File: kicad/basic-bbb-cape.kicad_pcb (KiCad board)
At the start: 2 copper layers, 54.6 x 86.4 mm, 2 parts, among them P8 BeagleBone_Black_Header, P9 BeagleBone_Black_Header

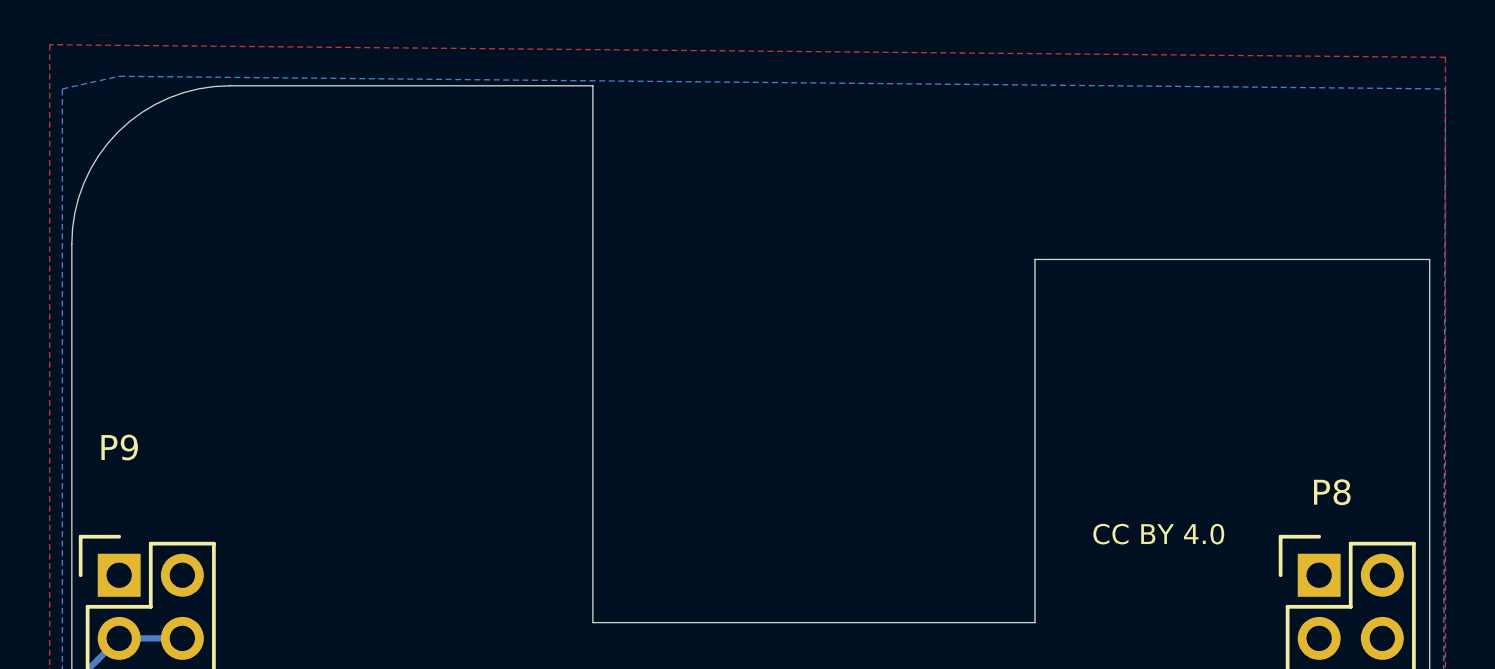
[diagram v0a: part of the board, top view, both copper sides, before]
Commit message: kicad: Multiple changes including adding
sym-lib-table,
Beaglebone_black_p8.kicad_sym, and
Beaglebone_black_p9.kicad_sym.
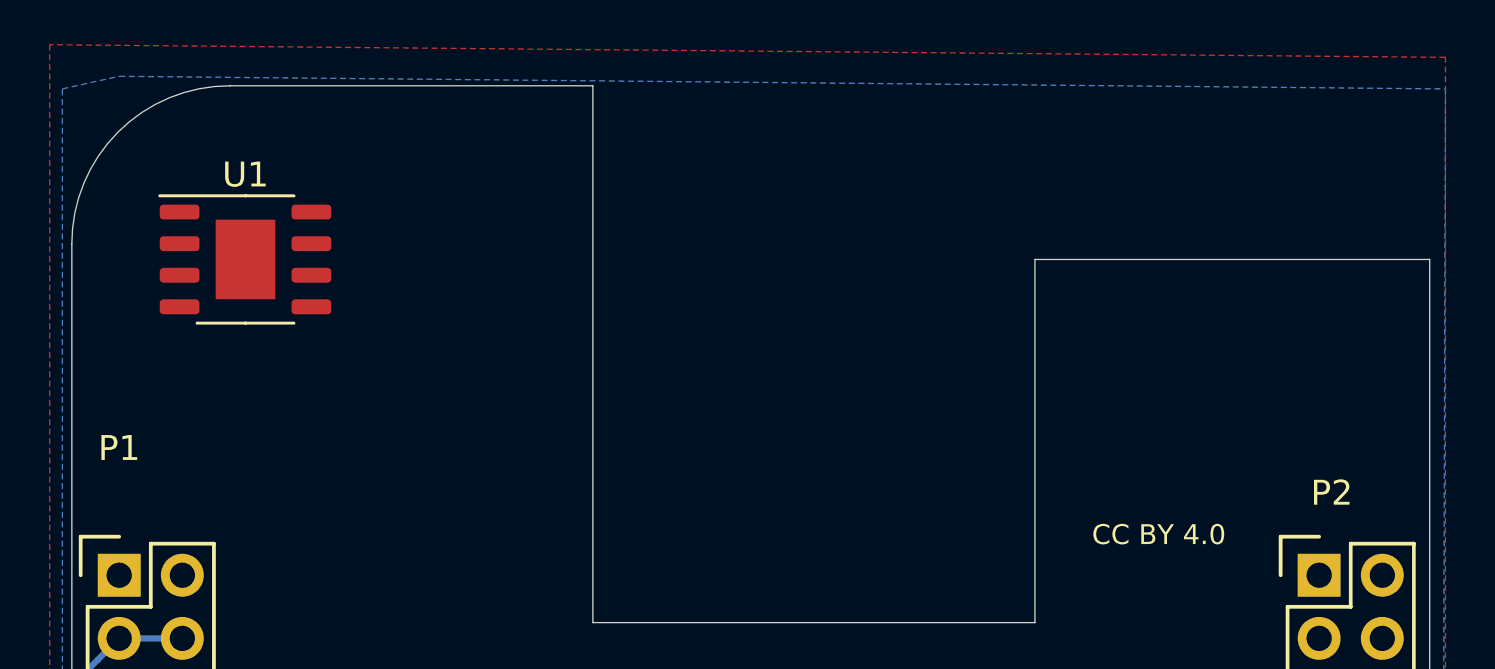
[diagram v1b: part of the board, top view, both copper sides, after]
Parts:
- added U1: CAT24C32YI-GT3, Package_SO:HTSOP-8-1EP_3.9x4.9mm_P1.27mm_EP2.4x3.2mm, F.Cu at (121.5, 49.7)
- renumbered P9 to P1, P8 to P2
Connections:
- P1 pad 10: Net-(P9-Pad10) -> unconnected-(P1-Pad10)
- P1 pad 11: Net-(P9-Pad11) -> unconnected-(P1-Pad11)
- P1 pad 12: Net-(P9-Pad12) -> unconnected-(P1-Pad12)
- P1 pad 13: Net-(P9-Pad13) -> unconnected-(P1-Pad13)
- P1 pad 14: Net-(P9-Pad14) -> unconnected-(P1-Pad14)
- P1 pad 15: Net-(P9-Pad15) -> unconnected-(P1-Pad15)
- P1 pad 16: Net-(P9-Pad16) -> unconnected-(P1-Pad16)
- P1 pad 17: Net-(P9-Pad17) -> unconnected-(P1-Pad17)
- P1 pad 18: Net-(P9-Pad18) -> unconnected-(P1-Pad18)
- P1 pad 19: Net-(P9-Pad19) -> unconnected-(P1-Pad19)
- P1 pad 20: Net-(P9-Pad20) -> unconnected-(P1-Pad20)
- P1 pad 21: Net-(P9-Pad21) -> unconnected-(P1-Pad21)
- P1 pad 22: Net-(P9-Pad22) -> unconnected-(P1-Pad22)
- P1 pad 23: Net-(P9-Pad23) -> unconnected-(P1-Pad23)
- P1 pad 24: Net-(P9-Pad24) -> unconnected-(P1-Pad24)
- P1 pad 25: Net-(P9-Pad25) -> unconnected-(P1-Pad25)
- P1 pad 26: Net-(P9-Pad26) -> unconnected-(P1-Pad26)
- P1 pad 27: Net-(P9-Pad27) -> unconnected-(P1-Pad27)
- P1 pad 28: Net-(P9-Pad28) -> unconnected-(P1-Pad28)
- P1 pad 29: Net-(P9-Pad29) -> unconnected-(P1-Pad29)
- P1 pad 30: Net-(P9-Pad30) -> unconnected-(P1-Pad30)
- P1 pad 31: Net-(P9-Pad31) -> unconnected-(P1-Pad31)
- P1 pad 33: Net-(P9-Pad33) -> unconnected-(P1-Pad33)
- P1 pad 35: Net-(P9-Pad35) -> unconnected-(P1-Pad35)
- P1 pad 36: Net-(P9-Pad36) -> unconnected-(P1-Pad36)
- P1 pad 37: Net-(P9-Pad37) -> unconnected-(P1-Pad37)
- P1 pad 38: Net-(P9-Pad38) -> unconnected-(P1-Pad38)
- P1 pad 39: Net-(P9-Pad39) -> unconnected-(P1-Pad39)
- P1 pad 40: Net-(P9-Pad40) -> unconnected-(P1-Pad40)
- P1 pad 41: Net-(P9-Pad41) -> unconnected-(P1-Pad41)
- P1 pad 42: Net-(P9-Pad42) -> unconnected-(P1-Pad42)
- P1 pad 9: Net-(P9-Pad9) -> unconnected-(P1-Pad9)
- P2 pad 10: Net-(P8-Pad10) -> unconnected-(P2-Pad10)
- P2 pad 11: Net-(P8-Pad11) -> unconnected-(P2-Pad11)
- P2 pad 12: Net-(P8-Pad12) -> unconnected-(P2-Pad12)
- P2 pad 13: Net-(P8-Pad13) -> unconnected-(P2-Pad13)
- P2 pad 14: Net-(P8-Pad14) -> unconnected-(P2-Pad14)
- P2 pad 15: Net-(P8-Pad15) -> unconnected-(P2-Pad15)
- P2 pad 16: Net-(P8-Pad16) -> unconnected-(P2-Pad16)
- P2 pad 17: Net-(P8-Pad17) -> unconnected-(P2-Pad17)
- P2 pad 18: Net-(P8-Pad18) -> unconnected-(P2-Pad18)
- P2 pad 19: Net-(P8-Pad19) -> unconnected-(P2-Pad19)
- P2 pad 20: Net-(P8-Pad20) -> unconnected-(P2-Pad20)
- P2 pad 21: Net-(P8-Pad21) -> unconnected-(P2-Pad21)
- P2 pad 22: Net-(P8-Pad22) -> unconnected-(P2-Pad22)
- P2 pad 23: Net-(P8-Pad23) -> unconnected-(P2-Pad23)
- P2 pad 24: Net-(P8-Pad24) -> unconnected-(P2-Pad24)
- P2 pad 25: Net-(P8-Pad25) -> unconnected-(P2-Pad25)
- P2 pad 26: Net-(P8-Pad26) -> unconnected-(P2-Pad26)
- P2 pad 27: Net-(P8-Pad27) -> unconnected-(P2-Pad27)
- P2 pad 28: Net-(P8-Pad28) -> unconnected-(P2-Pad28)
- P2 pad 29: Net-(P8-Pad29) -> unconnected-(P2-Pad29)
- P2 pad 3: Net-(P8-Pad3) -> unconnected-(P2-Pad3)
- P2 pad 30: Net-(P8-Pad30) -> unconnected-(P2-Pad30)
- P2 pad 31: Net-(P8-Pad31) -> unconnected-(P2-Pad31)
- P2 pad 32: Net-(P8-Pad32) -> unconnected-(P2-Pad32)
- P2 pad 33: Net-(P8-Pad33) -> unconnected-(P2-Pad33)
- P2 pad 34: Net-(P8-Pad34) -> unconnected-(P2-Pad34)
- P2 pad 35: Net-(P8-Pad35) -> unconnected-(P2-Pad35)
- P2 pad 36: Net-(P8-Pad36) -> unconnected-(P2-Pad36)
- P2 pad 37: Net-(P8-Pad37) -> unconnected-(P2-Pad37)
- P2 pad 38: Net-(P8-Pad38) -> unconnected-(P2-Pad38)
- P2 pad 39: Net-(P8-Pad39) -> unconnected-(P2-Pad39)
- P2 pad 4: Net-(P8-Pad4) -> unconnected-(P2-Pad4)
- P2 pad 40: Net-(P8-Pad40) -> unconnected-(P2-Pad40)
- P2 pad 41: Net-(P8-Pad41) -> unconnected-(P2-Pad41)
- P2 pad 42: Net-(P8-Pad42) -> unconnected-(P2-Pad42)
- P2 pad 43: Net-(P8-Pad43) -> unconnected-(P2-Pad43)
- P2 pad 44: Net-(P8-Pad44) -> unconnected-(P2-Pad44)
- P2 pad 45: Net-(P8-Pad45) -> unconnected-(P2-Pad45)
- P2 pad 46: Net-(P8-Pad46) -> unconnected-(P2-Pad46)
- P2 pad 5: Net-(P8-Pad5) -> unconnected-(P2-Pad5)
- P2 pad 6: Net-(P8-Pad6) -> unconnected-(P2-Pad6)
- P2 pad 7: Net-(P8-Pad7) -> unconnected-(P2-Pad7)
- P2 pad 8: Net-(P8-Pad8) -> unconnected-(P2-Pad8)
- P2 pad 9: Net-(P8-Pad9) -> unconnected-(P2-Pad9)
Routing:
- net unconnected-(P1-Pad23): track 0.00 -> 8.16 mm
- net Net-(P9-Pad23): track 8.16 -> 0.00 mm
- net unconnected-(P1-Pad17): track 0.00 -> 4.08 mm
- net Net-(P9-Pad17): track 4.08 -> 0.00 mm
- net unconnected-(P1-Pad21): track 0.00 -> 3.60 mm
- net Net-(P9-Pad21): track 3.60 -> 0.00 mm
- net unconnected-(P2-Pad13): track 0.00 -> 2.81 mm
- net Net-(P8-Pad13): track 2.81 -> 0.00 mm
- net unconnected-(P1-Pad16): track 0.00 -> 2.19 mm
- net Net-(P9-Pad16): track 2.19 -> 0.00 mm
- net unconnected-(P2-Pad18): track 0.00 -> 1.91 mm
- net Net-(P8-Pad18): track 1.91 -> 0.00 mm
- net unconnected-(P2-Pad19): track 0.00 -> 1.78 mm
- net Net-(P8-Pad19): track 1.78 -> 0.00 mm
- net unconnected-(P1-Pad15): track 0.00 -> 1.68 mm
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
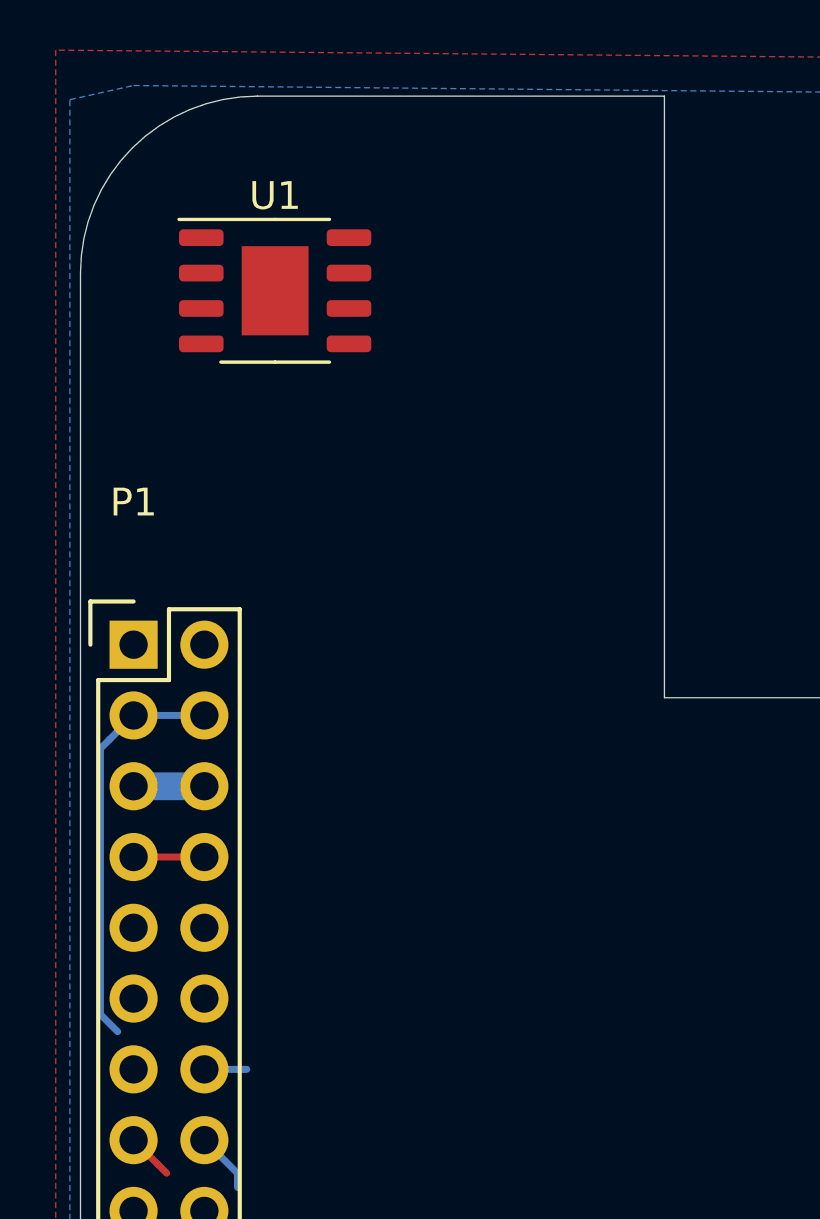
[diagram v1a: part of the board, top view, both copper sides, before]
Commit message: Placed RP on PCB; do not like it best to turn 180 degrees.
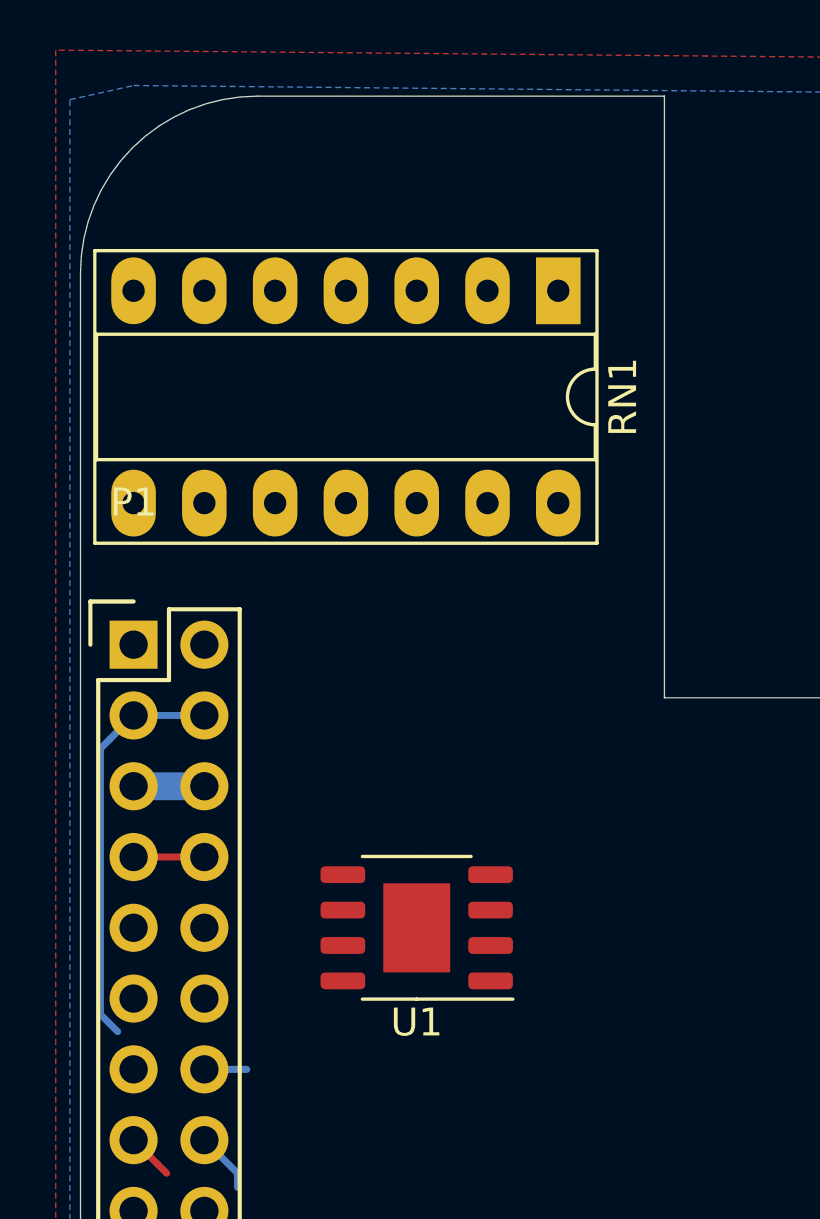
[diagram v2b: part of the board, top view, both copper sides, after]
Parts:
- added RN1: 5.6 k, Package_DIP:DIP-14_W7.62mm_Socket_LongPads, F.Cu at (131.6, 49.7)
- moved U1 23.4 mm to (126.5, 72.5), turned to 180 degrees
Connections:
- U1 pad 1: unconnected-(U1-Pad1) -> Net-(JP1-Pad2)
- U1 pad 2: unconnected-(U1-Pad2) -> Net-(JP2-Pad2)
- U1 pad 3: unconnected-(U1-Pad3) -> Net-(RN1-Pad12)
- U1 pad 4: unconnected-(U1-Pad4) -> GNDD
- U1 pad 5: unconnected-(U1-Pad5) -> I2C2_SDA
- U1 pad 6: unconnected-(U1-Pad6) -> I2C2_SCL
- U1 pad 7: unconnected-(U1-Pad7) -> Net-(RN1-Pad10)
- U1 pad 8: unconnected-(U1-Pad8) -> +3V3
